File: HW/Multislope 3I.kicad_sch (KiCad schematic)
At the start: 128 parts, among them J1 INT, J10 PWR, J11 TEST, J12 UART, J13 INPUT, J14 SLOPE, J15 PWR, J2 TEST, J3 COMP, J4 SLOT, J5 SLOT, J6 SLOT, J7 SLOPE2, J8 PWR, J9 SLOT, SW1 RST, U1 OPA21xx, U10 LM311, U11 NE5534, U12 OPA197, U14 431, U15 MCP3202, U16 Pico, U17 LM35, U18 ADuM121N, U2 LM399, U20 HT7533, U21 HT7550, U3 CD4053B, U4 OPA1xx, U5 OPA1xx, U6 OPA1xx, U7 431, U8 431, U9 408

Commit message: updated files
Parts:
- U3: value CD4053B -> SN74LV4053
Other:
- moved on the sheet: J1, J10, J11, J14, J3, J4, J5, J6, J7, J8, J9, N1

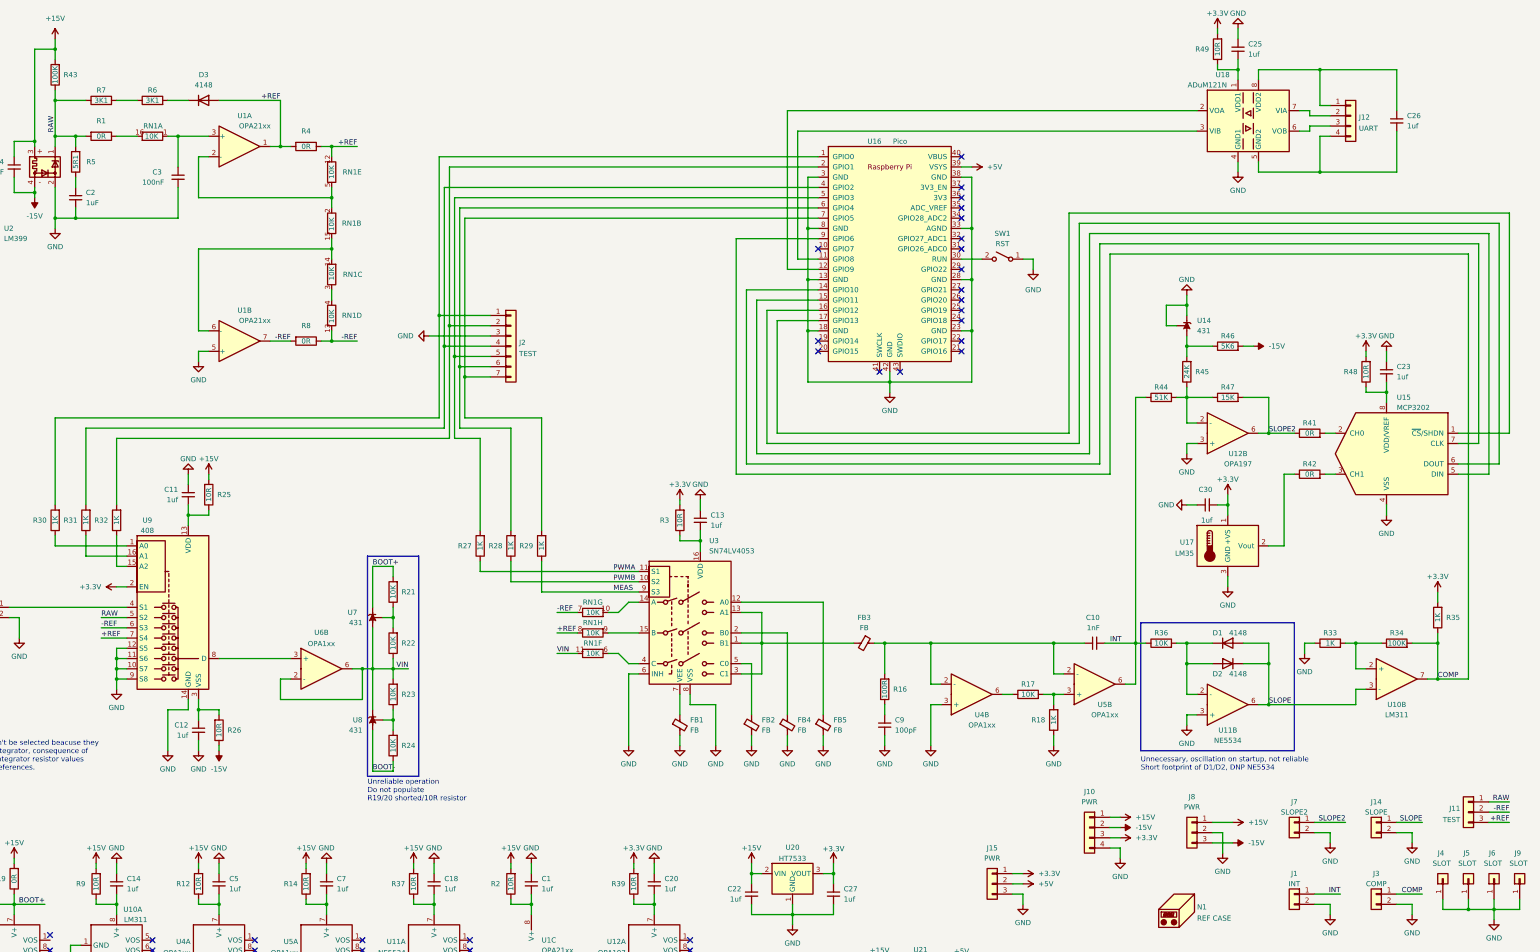
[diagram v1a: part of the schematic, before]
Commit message: Major code update 01.07.2024
Restarted work on finishing this project after more than a year.

Code was completely refactored. DMA/PIO interrupt was removed, and two state machines from the same PIO block were loaded with runup and (mock) residue code and sychronized using interrupt 0 (irq 0). Behaviour is exactly as expected. This is a huge step forward for this project.
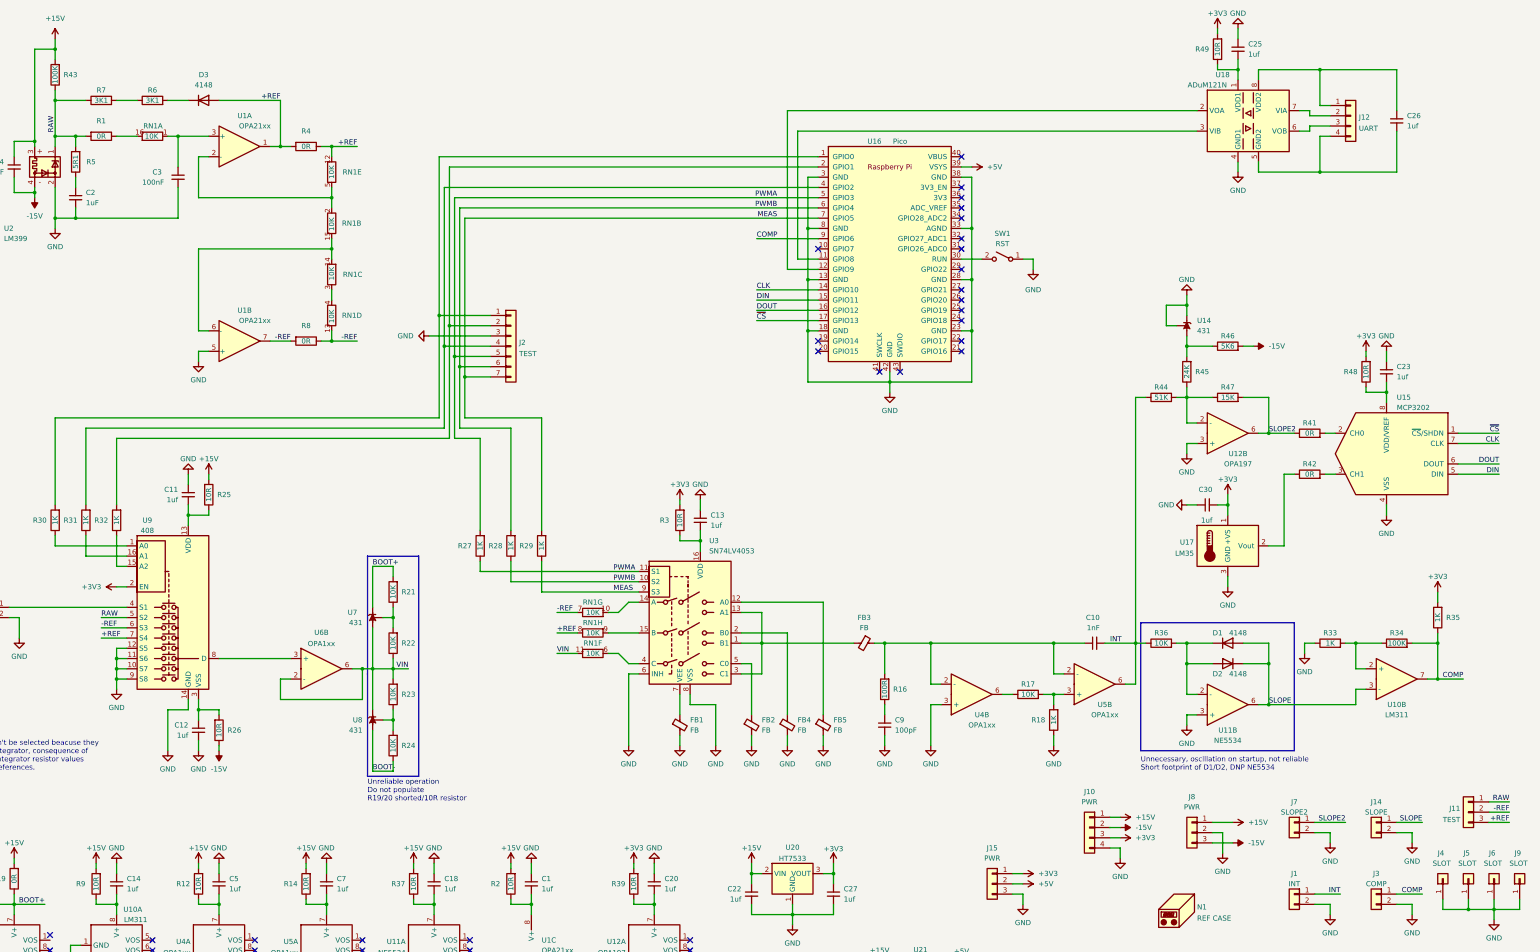
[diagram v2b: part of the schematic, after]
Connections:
- net MEAS: now also J2.7 (Pin_7), R29.2, U16.7 (GPIO5)
- net PWMA: now also J2.5 (Pin_5), R27.2, U16.5 (GPIO3)
- net PWMB: now also J2.6 (Pin_6), R28.2, U16.6 (GPIO4)
- net CLK: now reaches U15.7 (CLK), U16.14 (GPIO10)
- net DIN: now reaches U15.5 (DIN), U16.15 (GPIO11)
- net DOUT: now reaches U15.6 (DOUT), U16.16 (GPIO12)
- net ~{CS}: now reaches U15.1 (~{CS}/SHDN), U16.17 (GPIO13)
